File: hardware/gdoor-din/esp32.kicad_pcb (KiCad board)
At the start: 4 copper layers, 50 x 85 mm, 198 parts, among them J1 PlugIn_Terminal_Screw, J101 USB-C, J102 HR911105A, J103 EXP, J4 5V_IN, Q1 MMBT5401, Q2 MMBT2222A, SW101 TL3342, SW102 TL3342, U1 TLV9351, U101 ESP32-S3-WROOM-1-N8R2, U102 USBLC6-2SC6, U103 AMS1117-3.3, U104 W5500, U2 LMV321, U3 LMV321, U5 ES8374, U6 LM393, U7 AMS1117-3.3, Y101 25MHz

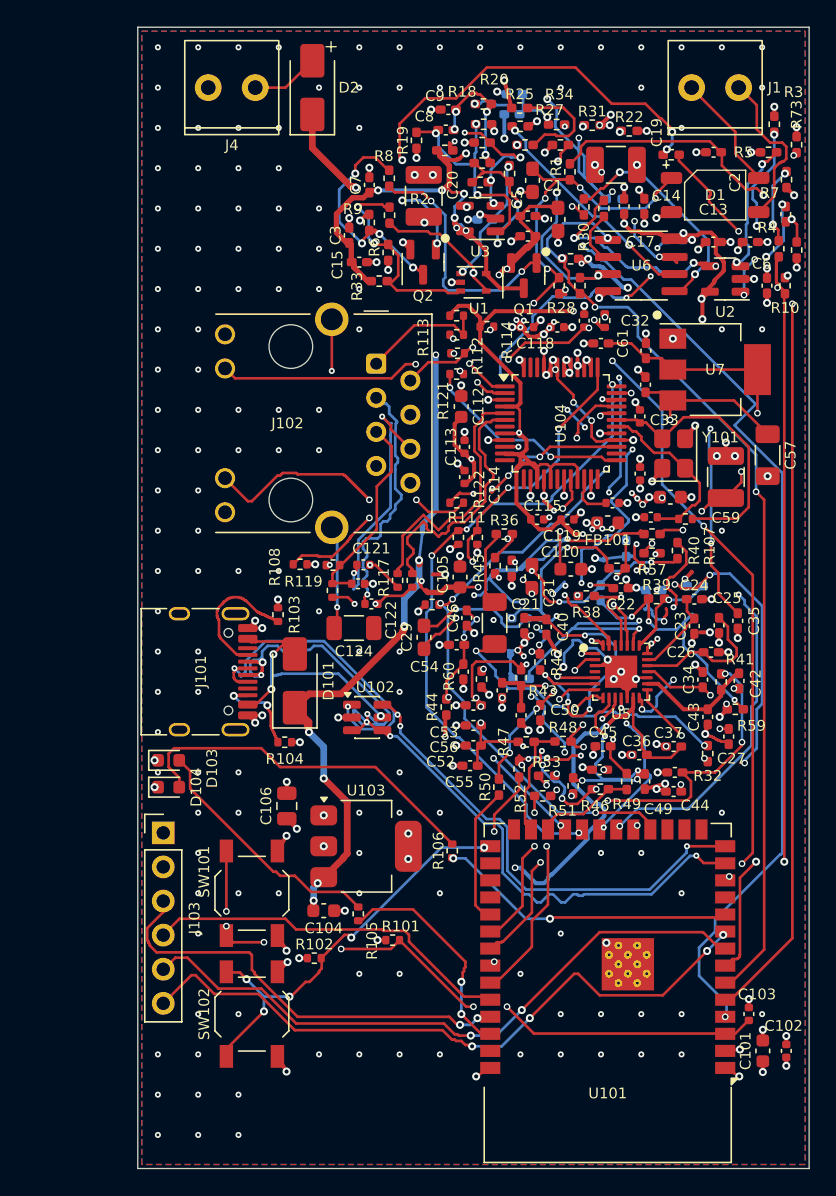
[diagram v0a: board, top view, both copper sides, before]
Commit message: gdoor-din: AP2114H regulator, front tab with flush RJ45 and USB-C
U103 (3.3 V digital) is now an AP2114H-3.3TRG1 (LCSC C150716): 1 A,
450 mV typ / 750 mV max dropout at 1 A, against about 1.1 V for the
AMS1117, so WiFi TX bursts do not brown out the S3. Same pinout as the
AMS1117 (1 GND, 2/tab VOUT, 3 VIN); the AP2114HA has a different one.
C104/C106 already meet the 4.7 uF minimum. JLC extended part.

The board gets a 6.8 x 40.4 mm front tab in the DIN window. J101 and
J102 move 8.45 mm forward (J102 also 0.8 mm down) with their Ethernet
and USB parts; their faces end 0.2 mm inside the window face. Tracks
crossing the moved block keep their shape and get connectors along the
move, so both halves of each pair grow equally (USB skew -4.20 mm, was
-4.17; Ethernet unchanged). 17 stitching vias under the moved parts are
gone. DRC: 0 errors, 0 unconnected, 0 parity issues.

Enclosure (first commit): 0.3 mm groove in the window wall for the tab,
body-sized RJ45 opening, tab in the fit-check ghost; fit check empty,
STLs rebuilt. JLC files and iBOMs regenerated (J101 CPL 97.09/-108.0).

Co-Authored-By: Claude Opus 5.5 <noreply@anthropic.com>
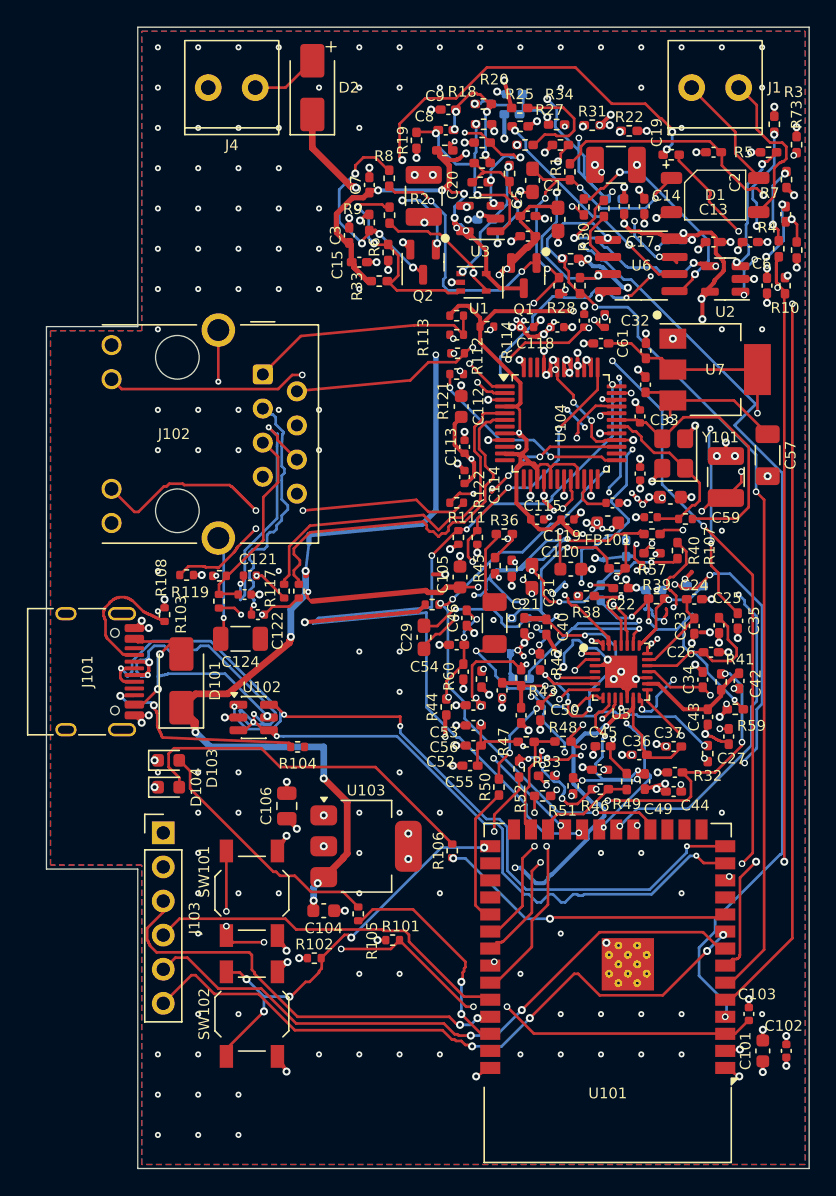
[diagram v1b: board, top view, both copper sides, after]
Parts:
- U103: value AMS1117-3.3 -> AP2114H-3.3TRG1
- moved C121 8.49 mm to (108.3, 100.8)
- moved C122 8.49 mm to (109.0, 103.8)
- moved C123 8.49 mm to (108.0, 102.2)
- moved J102 8.49 mm to (109.3, 85.9)
- moved R108 8.49 mm to (103.6, 100.8)
- moved R118 8.49 mm to (112.0, 102.0)
- moved R119 8.49 mm to (106.1, 100.9)
- moved R120 8.49 mm to (106.0, 102.8)
- moved C124 8.49 mm to (107.7, 105.5)
- moved R117 8.49 mm to (110.9, 102.0)
- moved D101 8.45 mm to (103.3, 108.7)
- moved J101 8.45 mm to (95.7, 108.0)
- moved U102 8.45 mm to (108.6, 111.4)
- moved R103 8.45 mm to (102.0, 103.8)
- moved R104 1.02 mm to (111.9, 113.6)
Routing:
- net +5V: track 123.2 -> 148.0 mm
- net /MCU, USB, Power, Ethernet/ETH_INT: track 49.0 -> 66.0 mm
- net /MCU, USB, Power, Ethernet/USB_CC2: track 6.94 -> 16.3 mm
- net /MCU, USB, Power, Ethernet/ETH_EXRES: track 21.6 -> 30.1 mm
- net +3.3V: track 71.7 -> 80.2 mm
- net /MCU, USB, Power, Ethernet/ETH_TCT: track 18.0 -> 26.5 mm
- net /MCU, USB, Power, Ethernet/ETH_TD_N: track 7.86 -> 16.3 mm
- net /MCU, USB, Power, Ethernet/ETH_ACTLED_K: track 23.4 -> 31.8 mm
- net /MCU, USB, Power, Ethernet/ETH_TD_P: track 9.37 -> 17.9 mm
- net /MCU, USB, Power, Ethernet/ETH_RXP_CHIP: track 19.7 -> 28.2 mm
- net /MCU, USB, Power, Ethernet/ETH_RXN_CHIP: track 19.4 -> 27.8 mm
- net /MCU, USB, Power, Ethernet/ETH_LINKLED_K: track 18.8 -> 27.3 mm
- net /MCU, USB, Power, Ethernet/USB_DN: track 66.5 -> 74.9 mm
- net /MCU, USB, Power, Ethernet/USB_DP: track 62.3 -> 70.7 mm
- net GND: track 134.1 -> 133.5 mm, vias 280 -> 262
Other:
- board size 50 x 85 mm -> 56.8 x 85 mm

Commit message: gdoor-din: logic check, drop unused options, flush USB-C cut-out
Logic check of the schematic against the netlist (ERC, block by block).
One real error: the BOOT/RESET labels were swapped. SW101 is EN (RESET),
SW102 is IO0 (BOOT). Fixed on the silkscreen and on the enclosure lid.

Removed the unfitted options that have no use on this board: R55
(+3.3V to +3.3V_AUDIO link), R56 (RX_DAC link), R69-R72 (mic
attenuation) and C62/C63 (alternative mic coupling), with their wiring
and their tracks (including a +3.3V_AUDIO run on In2.Cu that only served
R55). Netlist comparison: no remaining pin changed net. DRC: 0 errors,
0 unconnected. BOM and CPL unchanged (all were DNP).

Silkscreen labels RESET (SW101) and BOOT (SW102). Enclosure: the USB-C
opening is now a 9.4 x 3.7 mm stadium around the flush receptacle shell;
the fit check models the shell as a stadium too and is empty.

DESIGN.md rewritten: blocks, pin map, logic-check results, and open
points split into decisions (C10/R21/C18 DNP vs upstream, C29/C31 25 V
on the bus, 0 ohm links, J4/D2), KiCad to-dos (F8 for two renamed nets,
the RX_DAC bus entry) and first-build checks.

Co-Authored-By: Claude Opus 5.5 <noreply@anthropic.com>
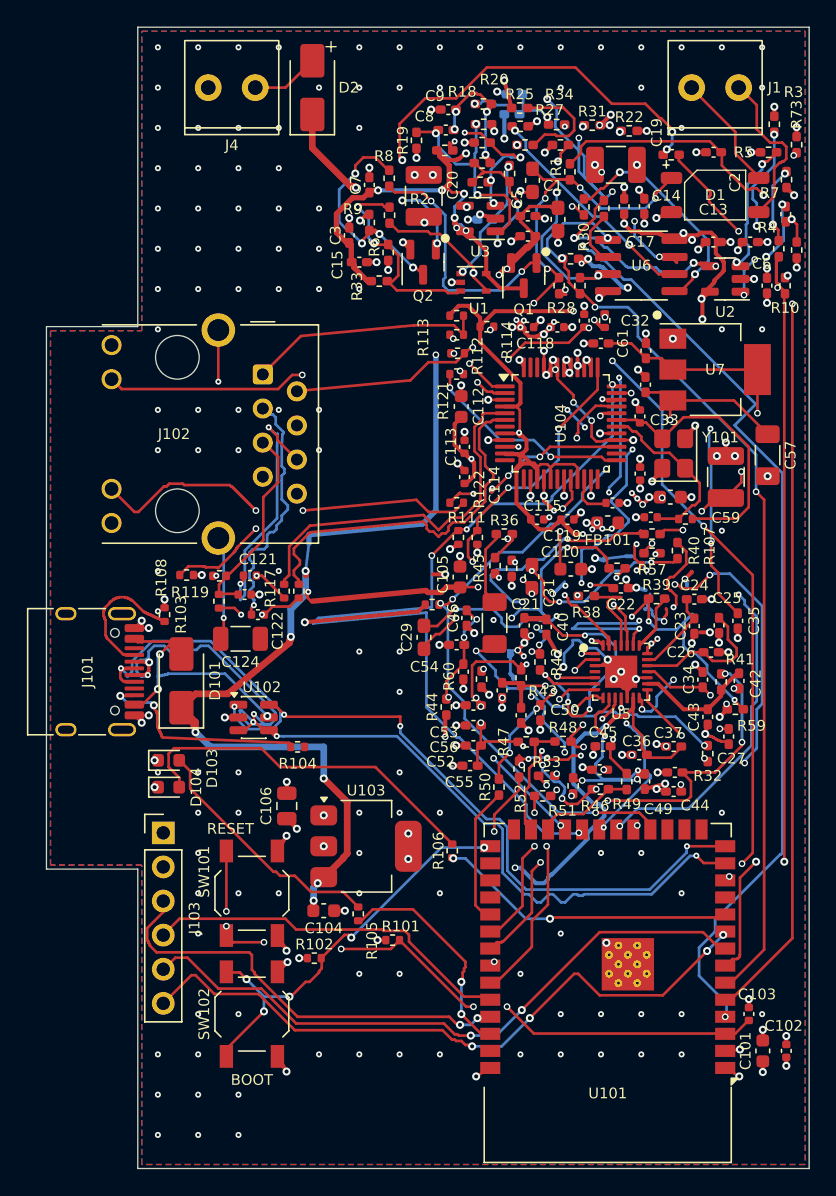
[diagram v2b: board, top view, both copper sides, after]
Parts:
- removed C62, C63: 100n, Library:C_0402_1005Metric_Pad0.74x0.62mm_HandSolder
- removed R55, R56: 0, Library:R_0402_1005Metric_Pad0.72x0.64mm_HandSolder
- removed R69, R70, R71, R72: 1k, Library:R_0402_1005Metric_Pad0.72x0.64mm_HandSolder
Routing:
- net +3.3V_AUDIO: track 130.6 -> 81.8 mm, vias 25 -> 20
- net Net-(U5A-MIC2P): track 25.9 -> 20.8 mm
- net Net-(U5A-MIC1P): track 10.1 -> 6.85 mm, vias 2 -> 0
- net Net-(U5A-MIC2N): track 11.0 -> 8.02 mm, vias 1 -> 0
- net Net-(C62-Pad1): track 20.0 -> 17.2 mm
- net Net-(U5A-MIC1N): track 8.59 -> 6.59 mm, vias 3 -> 2
- net +3.3V: track 80.2 -> 79.5 mm
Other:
- board text added: "BOOT"
- board text added: "RESET"

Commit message: gdoor-din: 50 V bus caps, fit C10/R21 on the front
C29 and C31 sit on the bus DC (up to about 30 V) through R74 and were
25 V parts. C29 is now 10 uF 50 V 1206 (C13585, like C21); C31 is
10 uF 50 V 0805 (C440198), since a 1206 does not fit at its spot. C31's
pad-1 route to R40 is re-routed down its right side.

C10 (1 nF) and R21 (4k7) on the TX node are fitted on the upstream
board but were DNP on B.Cu here. They are now on F.Cu, fitted by JLC,
joined to the old TX-node track by a via, with their own GND vias.
C18 (100 pF, TX driver input) has no free F.Cu spot and stays on B.Cu
for hand soldering.

Schematic: C10/R21 no longer DNP, the leftover RX_DAC bus entry is
removed; ERC has no errors. DRC: 0 errors, 0 unconnected, 0 parity.
JLC files regenerated: BOM 62 lines, CPL 186 parts.

Co-Authored-By: Claude Opus 5.5 <noreply@anthropic.com>
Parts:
- C10, R21: moved to F.Cu
- C29: footprint Library:C_0603_1608Metric_Pad1.08x0.95mm_HandSolder -> Capacitor_SMD:C_1206_3216Metric
- C31: footprint Library:C_0603_1608Metric_Pad1.08x0.95mm_HandSolder -> Capacitor_SMD:C_0805_2012Metric
- moved C10 4.03 mm to (131.2, 64.3), turned to 180 degrees
- moved C29 1.12 mm to (120.6, 106.3)
- moved R21 1.09 mm to (128.9, 64.3)
- moved C31 0.42 mm to (129.4, 100.5)
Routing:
- net Net-(C10-Pad2): track 7.96 -> 9.74 mm, vias 2 -> 3
- net Net-(C29-Pad2): track 23.8 -> 25.3 mm
- net GND: track 133.5 -> 132.5 mm, vias 262 -> 263
- net Net-(C31-Pad1): track 19.7 -> 20.4 mm
